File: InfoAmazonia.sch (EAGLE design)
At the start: 72 parts, among them IC1 LM2662, IC11 74HC4051, IC2 ADAFRUIT FONA, IC3 MIC29302AWD, IC4 4050D, IC5 TL032C, IC6 CA3140AM Z, IC7 TL081BCDG4, IC8 SHT20, IC9 NE555, J1 BNCPTH, J2 BNCPTH, J3 BNCPTH, U1 ARDUINO-MEGAPRO, U2 MPL3115A2, U3 USD-SOCKETNEW, U4 ALS-PT19

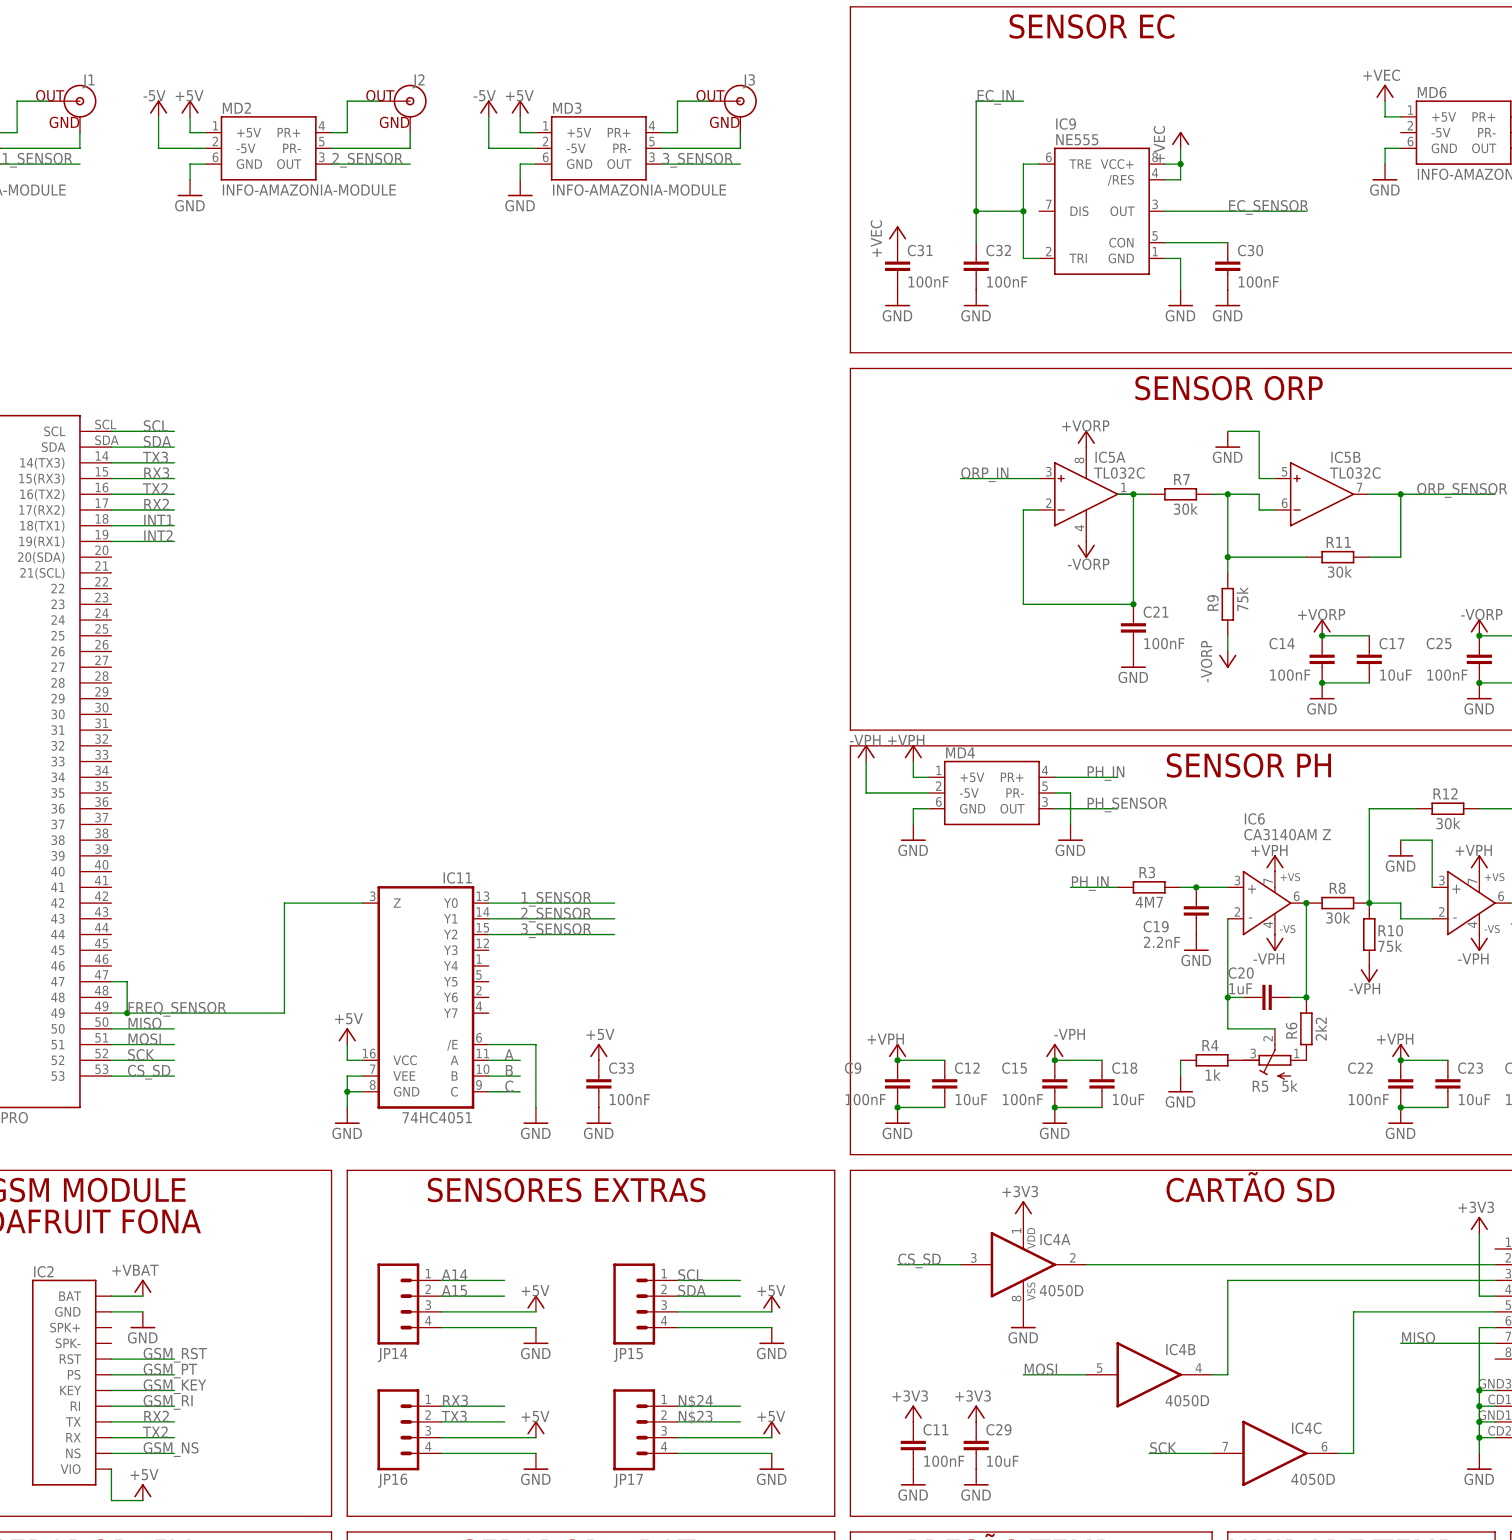
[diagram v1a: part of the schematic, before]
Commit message: - Roteado os sensores do lado
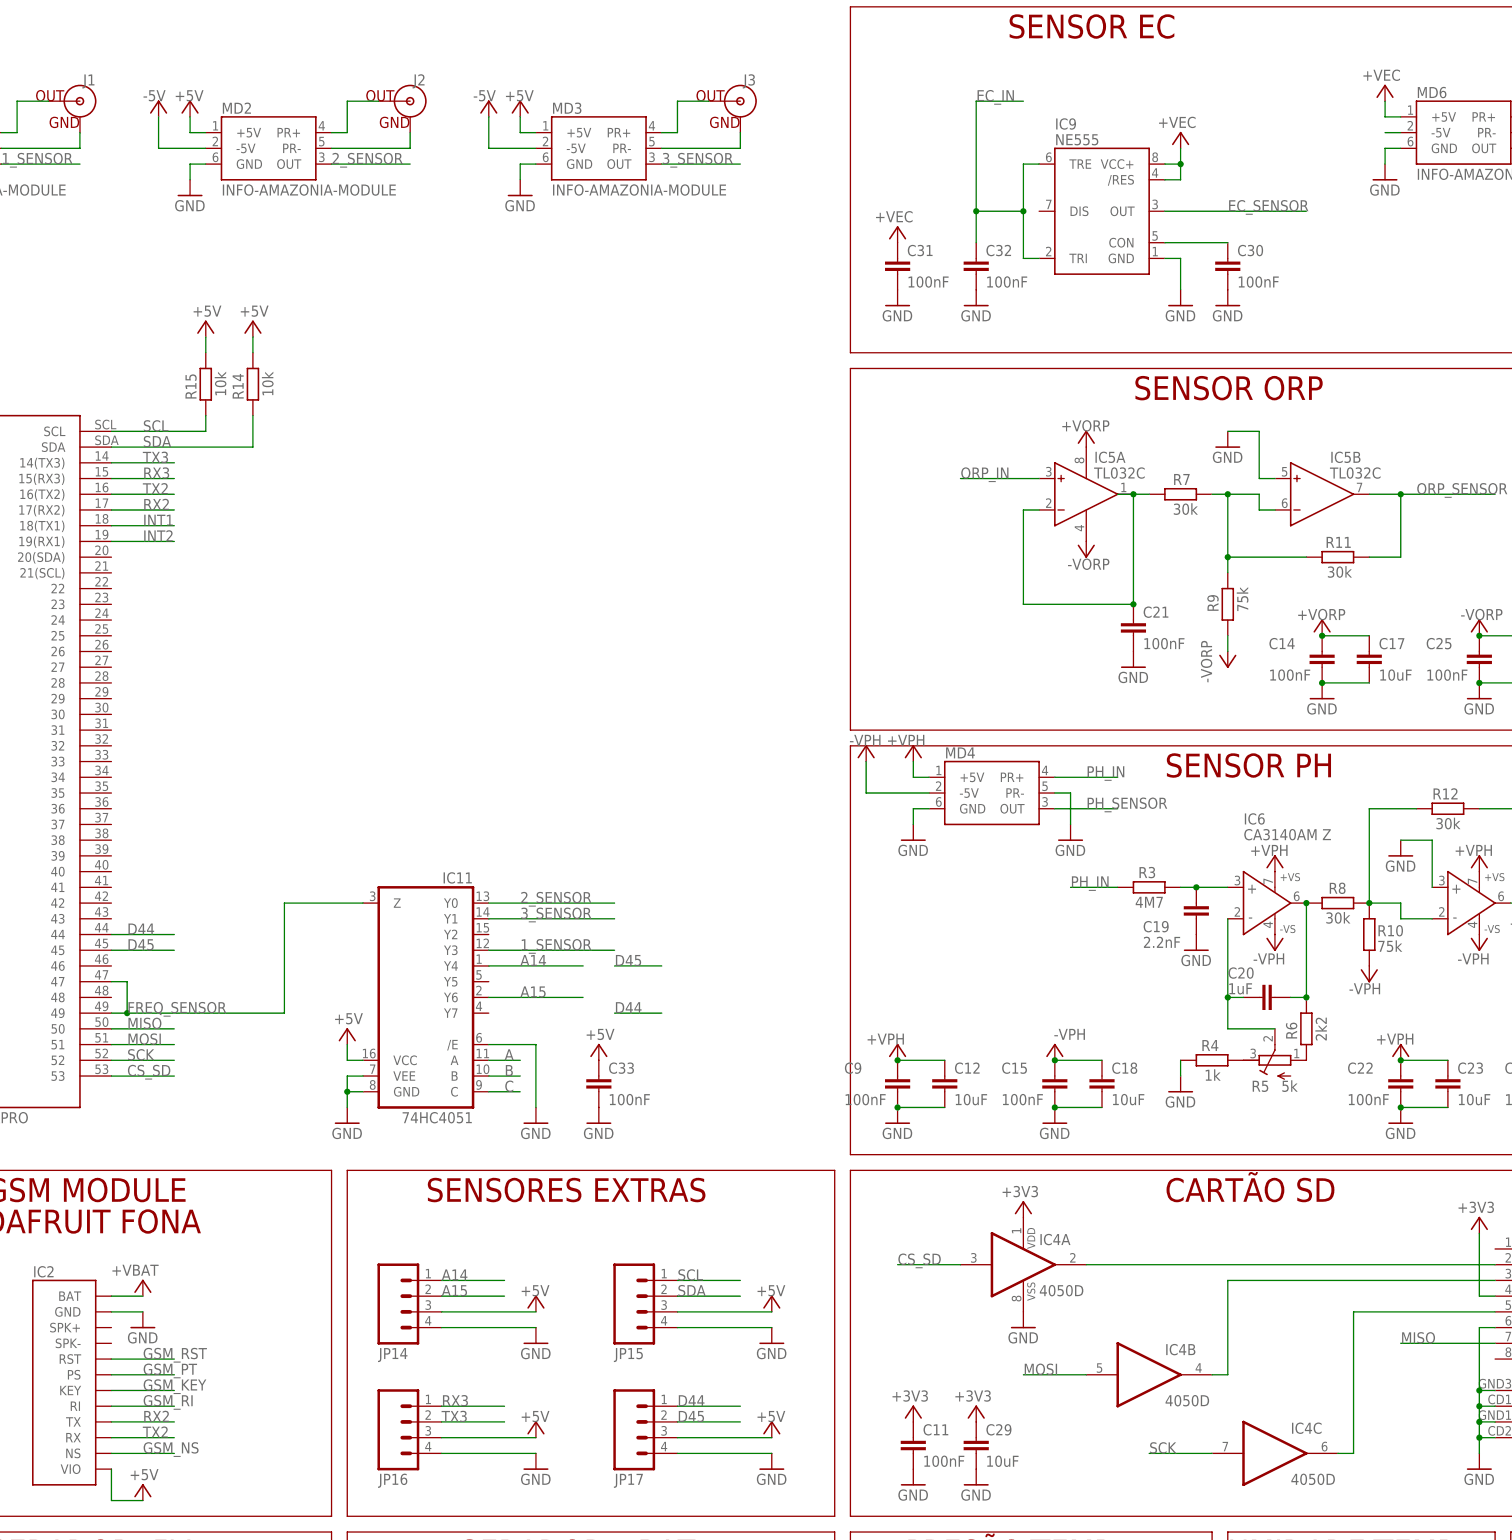
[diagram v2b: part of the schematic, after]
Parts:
- added R14, R15: 10k, InfoAmazonia:R-EU_R0603
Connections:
- removed net N$24: JP17.1
- new net D44: JP17.1, U1.44
- new net D45: JP17.2, U1.45
- net +5V: now also R14.2, R15.2
- net 1_SENSOR: now also IC11.Y3; no longer IC11.Y0
- net 2_SENSOR: now also IC11.Y0; no longer IC11.Y1
- net 3_SENSOR: now also IC11.Y1; no longer IC11.Y2
- net A14: now also IC11.Y4
- net A15: now also IC11.Y6
- net N$23: now also MD6.-5V; no longer JP17.2
- net SCL: now also R15.1
- net SDA: now also R14.1
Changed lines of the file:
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@@
 <part name="P+10" library="InfoAmazonia" deviceset="+5V" device=""/>
 <part name="GND49" library="InfoAmazonia" deviceset="GND" device=""/>
+<part name="R15" library="InfoAmazonia" deviceset="R-EU_" device="R0603" value="10k"/>
+<part name="R14" library="InfoAmazonia" deviceset="R-EU_" device="R0603" value="10k"/>
+<part name="P+14" library="InfoAmazonia" deviceset="+5V" device=""/>
+<part name="P+18" library="InfoAmazonia" deviceset="+5V" device=""/>
 </parts>
 <sheets>
@@
 </instance>
 <instance part="P+7" gate="G$1" x="170.18" y="137.16" smashed="yes">
-<attribute name="VALUE" x="167.64" y="132.08" size="1.778" layer="96" rot="R90"/>
+<attribute name="VALUE" x="172.72" y="139.7" size="1.778" layer="96" rot="R180"/>
 </instance>
 <instance part="P+15" gate="G$1" x="124.46" y="121.92" smashed="yes">
-<attribute name="VALUE" x="121.92" y="116.84" size="1.778" layer="96" rot="R90"/>
+<attribute name="VALUE" x="127" y="124.46" size="1.778" layer="96" rot="R180"/>
 </instance>
 <instance part="P-9" gate="G$1" x="218.44" y="5.08" smashed="yes">
@@
 <instance part="GND49" gate="1" x="76.2" y="-22.86" smashed="yes">
 <attribute name="VALUE" x="73.66" y="-25.4" size="1.778" layer="96"/>
+</instance>
+<instance part="R15" gate="G$1" x="12.7" y="96.52" smashed="yes" rot="R90">
+<attribute name="NAME" x="11.2014" y="93.98" size="1.778" layer="95" rot="R90"/>
+<attribute name="VALUE" x="16.002" y="94.488" size="1.778" layer="96" rot="R90"/>
+</instance>
+<instance part="R14" gate="G$1" x="20.32" y="96.52" smashed="yes" rot="R90">
+<attribute name="NAME" x="18.8214" y="93.98" size="1.778" layer="95" rot="R90"/>
+<attribute name="VALUE" x="23.622" y="94.488" size="1.778" layer="96" rot="R90"/>
+</instance>
+<instance part="P+14" gate="1" x="12.7" y="106.68" smashed="yes">
+<attribute name="VALUE" x="15.24" y="109.22" size="1.778" layer="96" rot="R180"/>
+</instance>
+<instance part="P+18" gate="1" x="20.32" y="106.68" smashed="yes">
+<attribute name="VALUE" x="22.86" y="109.22" size="1.778" layer="96" rot="R180"/>
 </instance>
 </instances>
@@
 <pinref part="P+10" gate="1" pin="+5V"/>
 </segment>
+<segment>
+<pinref part="R15" gate="G$1" pin="2"/>
+<pinref part="P+14" gate="1" pin="+5V"/>
+<wire x1="12.7" y1="101.6" x2="12.7" y2="104.14" width="0.1524" layer="91"/>
+</segment>
+<segment>
+<pinref part="R14" gate="G$1" pin="2"/>
+<pinref part="P+18" gate="1" pin="+5V"/>
+<wire x1="20.32" y1="101.6" x2="20.32" y2="104.14" width="0.1524" layer="91"/>
+</segment>
 </net>
 <net name="+3V3" class="0">
@@
 <segment>
 <pinref part="U1" gate="G$1" pin="SDA"/>
-<wire x1="-2.54" y1="86.36" x2="7.62" y2="86.36" width="0.1524" layer="91"/>
 <label x="2.54" y="86.36" size="1.778" layer="95"/>
+<pinref part="R14" gate="G$1" pin="1"/>
+<wire x1="-2.54" y1="86.36" x2="20.32" y2="86.36" width="0.1524" layer="91"/>
+<wire x1="20.32" y1="86.36" x2="20.32" y2="91.44" width="0.1524" layer="91"/>
 </segment>
 <segment>
@@
 <segment>
 <pinref part="U1" gate="G$1" pin="SCL"/>
-<wire x1="-2.54" y1="88.9" x2="7.62" y2="88.9" width="0.1524" layer="91"/>
+<wire x1="-2.54" y1="88.9" x2="12.7" y2="88.9" width="0.1524" layer="91"/>
 <label x="2.54" y="88.9" size="1.778" layer="95"/>
+<pinref part="R15" gate="G$1" pin="1"/>
+<wire x1="12.7" y1="88.9" x2="12.7" y2="91.44" width="0.1524" layer="91"/>
 </segment>
 <segment>
@@
 </segment>
 <segment>
-<wire x1="58.42" y1="12.7" x2="78.74" y2="12.7" width="0.1524" layer="91"/>
-<label x="63.5" y="12.7" size="1.778" layer="95"/>
-<pinref part="IC11" gate="A" pin="Y0"/>
+<pinref part="IC11" gate="A" pin="Y3"/>
+<wire x1="58.42" y1="5.08" x2="78.74" y2="5.08" width="0.1524" layer="91"/>
+<label x="63.5" y="5.08" size="1.778" layer="95"/>
 </segment>
 </net>
@@
 </segment>
 <segment>
-<wire x1="58.42" y1="10.16" x2="78.74" y2="10.16" width="0.1524" layer="91"/>
-<label x="63.5" y="10.16" size="1.778" layer="95"/>
-<pinref part="IC11" gate="A" pin="Y1"/>
-</segment>
-<segment>
 <pinref part="MD2" gate="G$1" pin="OUT"/>
 <wire x1="33.02" y1="132.08" x2="45.72" y2="132.08" width="0.1524" layer="91"/>
 <label x="33.02" y="132.08" size="1.778" layer="95"/>
 </segment>
+<segment>
+<pinref part="IC11" gate="A" pin="Y0"/>
+<wire x1="58.42" y1="12.7" x2="78.74" y2="12.7" width="0.1524" layer="91"/>
+<label x="63.5" y="12.7" size="1.778" layer="95"/>
+</segment>
 </net>
 <net name="3_SENSOR" class="0">
@@
 </segment>
 <segment>
-<wire x1="58.42" y1="7.62" x2="78.74" y2="7.62" width="0.1524" layer="91"/>
-<label x="63.5" y="7.62" size="1.778" layer="95"/>
-<pinref part="IC11" gate="A" pin="Y2"/>
-</segment>
-<segment>
 <pinref part="MD3" gate="G$1" pin="OUT"/>
 <wire x1="86.36" y1="132.08" x2="99.06" y2="132.08" width="0.1524" layer="91"/>
 <label x="86.36" y="132.08" size="1.778" layer="95"/>
 </segment>
+<segment>
+<pinref part="IC11" gate="A" pin="Y1"/>
+<wire x1="58.42" y1="10.16" x2="78.74" y2="10.16" width="0.1524" layer="91"/>
+<label x="63.5" y="10.16" size="1.778" layer="95"/>
+</segment>
 </net>
 <net name="A15" class="0">
@@
 <label x="-66.04" y="30.48" size="1.778" layer="95"/>
 </segment>
+<segment>
+<label x="63.5" y="-2.54" size="1.778" layer="95"/>
+<wire x1="73.66" y1="-2.54" x2="58.42" y2="-2.54" width="0.1524" layer="91"/>
+<pinref part="IC11" gate="A" pin="Y6"/>
+</segment>
 </net>
 <net name="A14" class="0">
@@
 <wire x1="-43.18" y1="33.02" x2="-66.04" y2="33.02" width="0.1524" layer="91"/>
 <label x="-66.04" y="33.02" size="1.778" layer="95"/>
+</segment>
+<segment>
+<label x="63.5" y="2.54" size="1.778" layer="95"/>
+<wire x1="73.66" y1="2.54" x2="58.42" y2="2.54" width="0.1524" layer="91"/>
+<pinref part="IC11" gate="A" pin="Y4"/>
 </segment>
 </net>
@@
 </segment>
 </net>
-<net name="N$23" class="0">
+<net name="D44" class="0">
+<segment>
+<pinref part="U1" gate="G$1" pin="44"/>
+<wire x1="-2.54" y1="7.62" x2="7.62" y2="7.62" width="0.1524" layer="91"/>
+<label x="0" y="7.62" size="1.778" layer="95"/>
+</segment>
+<segment>
+<pinref part="JP17" gate="G$1" pin="1"/>
+<wire x1="88.9" y1="-68.58" x2="99.06" y2="-68.58" width="0.1524" layer="91"/>
+<label x="88.9" y="-68.58" size="1.778" layer="95"/>
+</segment>
+<segment>
+<label x="78.74" y="-5.08" size="1.778" layer="95"/>
+<wire x1="86.36" y1="-5.08" x2="78.74" y2="-5.08" width="0.1524" layer="91"/>
+</segment>
+</net>
+<net name="D45" class="0">
+<segment>
+<pinref part="U1" gate="G$1" pin="45"/>
+<wire x1="-2.54" y1="5.08" x2="7.62" y2="5.08" width="0.1524" layer="91"/>
+<label x="0" y="5.08" size="1.778" layer="95"/>
+</segment>
 <segment>
 <pinref part="JP17" gate="G$1" pin="2"/>
@@
 <label x="88.9" y="-71.12" size="1.778" layer="95"/>
 </segment>
-</net>
-<net name="N$24" class="0">
-<segment>
-<pinref part="JP17" gate="G$1" pin="1"/>
-<wire x1="88.9" y1="-68.58" x2="99.06" y2="-68.58" width="0.1524" layer="91"/>
-<label x="88.9" y="-68.58" size="1.778" layer="95"/>
-</segment>
-</net>
+<segment>
+<label x="78.74" y="2.54" size="1.778" layer="95"/>
+<wire x1="86.36" y1="2.54" x2="78.74" y2="2.54" width="0.1524" layer="91"/>
+</segment>
+</net>
+<net name="N$23" class="0">
+<segment>
+<pinref part="MD6" gate="G$1" pin="-5V"/>
+<wire x1="205.74" y1="137.16" x2="203.2" y2="137.16" width="0.1524" layer="91"/>
+</segment>
+</net>

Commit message: - Adicionado o controlador de tensões, falta rotear
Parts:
- removed MD2, MD3: INFO-AMAZONIA-MODULE, InfoAmazonia:INFO-AMAZONIA-MODULE
- added C10, C34, C35, C36, C37, C38: 100nF, InfoAmazonia:C-EUC0603
- added IC10, IC12, IC13: 4053D, InfoAmazonia:4053D
- added MD7, MD8: INFO-AMAZONIA-MODULE, InfoAmazonia:INFO-AMAZONIA-MODULE
- IC11: device InfoAmazonia:4051PW -> InfoAmazonia:4051D
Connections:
- new net 1_SENSOR_EN: IC10.A, IC10.B, IC10.C
- new net 2_SENSOR_EN: IC12.A, IC12.B, IC12.C
- new net 3_SENSOR_EN: IC13.A, IC13.B, IC13.C
- new net N$24: IC10.X0, MD1.+5V
- new net N$25: IC10.Y0, MD1.-5V
- new net N$26: IC10.Z0, MD1.GND
- new net N$27: IC12.Z0, MD7.GND
- new net N$28: IC12.Y0, MD7.-5V
- new net N$29: IC12.X0, MD7.+5V
- new net N$30: IC13.X0, MD8.+5V
- new net N$31: IC13.Y0, MD8.-5V
- new net N$32: IC13.Z0, MD8.GND
- net +5V: now also C34.1, C36.1, C38.1, IC10.VCC, IC10.X, IC12.VCC, IC12.X, IC13.VCC, IC13.X; no longer MD1.+5V, MD2.+5V, MD3.+5V
- net -5V: now also C10.1, C35.1, C37.1, IC10.VEE, IC10.Y, IC12.VEE, IC12.Y, IC13.VEE, IC13.Y; no longer MD1.-5V, MD2.-5V, MD3.-5V
- net 1_SENSOR: now also U1.A10; no longer U1.A2
- net 2_SENSOR: now also MD7.OUT, U1.A11; no longer MD2.OUT, U1.A3
- net 3_SENSOR: now also MD8.OUT, U1.A12; no longer MD3.OUT, U1.A4
- net GND: now also C10.2, C34.2, C35.2, C36.2, C37.2, C38.2, IC10./E, IC10.GND, IC10.Z, IC12./E, IC12.GND, IC12.Z, IC13./E, IC13.GND, IC13.Z; no longer MD1.GND, MD2.GND, MD3.GND
- net LUZ_SENSOR: now also U1.A13; no longer U1.A5
- net N$11: now also MD7.PR-; no longer MD2.PR-
- net N$12: now also MD7.PR+; no longer MD2.PR+
- net N$13: now also MD8.PR-; no longer MD3.PR-
- net N$22: now also MD8.PR+; no longer MD3.PR+
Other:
- moved on the sheet: C12, C14, C15, C17, C18, C19, C20, C21, C22, C23, C24, C25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
